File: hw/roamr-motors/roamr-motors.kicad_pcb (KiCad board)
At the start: 2 copper layers, 115 x 55 mm, 82 parts, among them J1 USB_C_Receptacle_USB2.0_14P, J10 JST_XH_S2B-XH-A-1, J2 USB_C_Receptacle_USB2.0_14P, J3 JST_XH_S2B-XH-A-1, J4 JST_XH_S2B-XH-A-1, J5 JST_PH_B3B-PH-SM4-TB, J6 JST_PH_B3B-PH-SM4-TB, J7 JST_SH_BM06B-SRSS-TB, J8 JST_SH_BM06B-SRSS-TB, J9 JST_XH_S2B-XH-A-1, U1 DRV8316CRRGFR, U2 DRV8316CRRGFR, U3 ESP32-S3-WROOM-1, U4 CP2102N-A02-GQFN28, U5 SGM2212-3.3XKC3G_TR

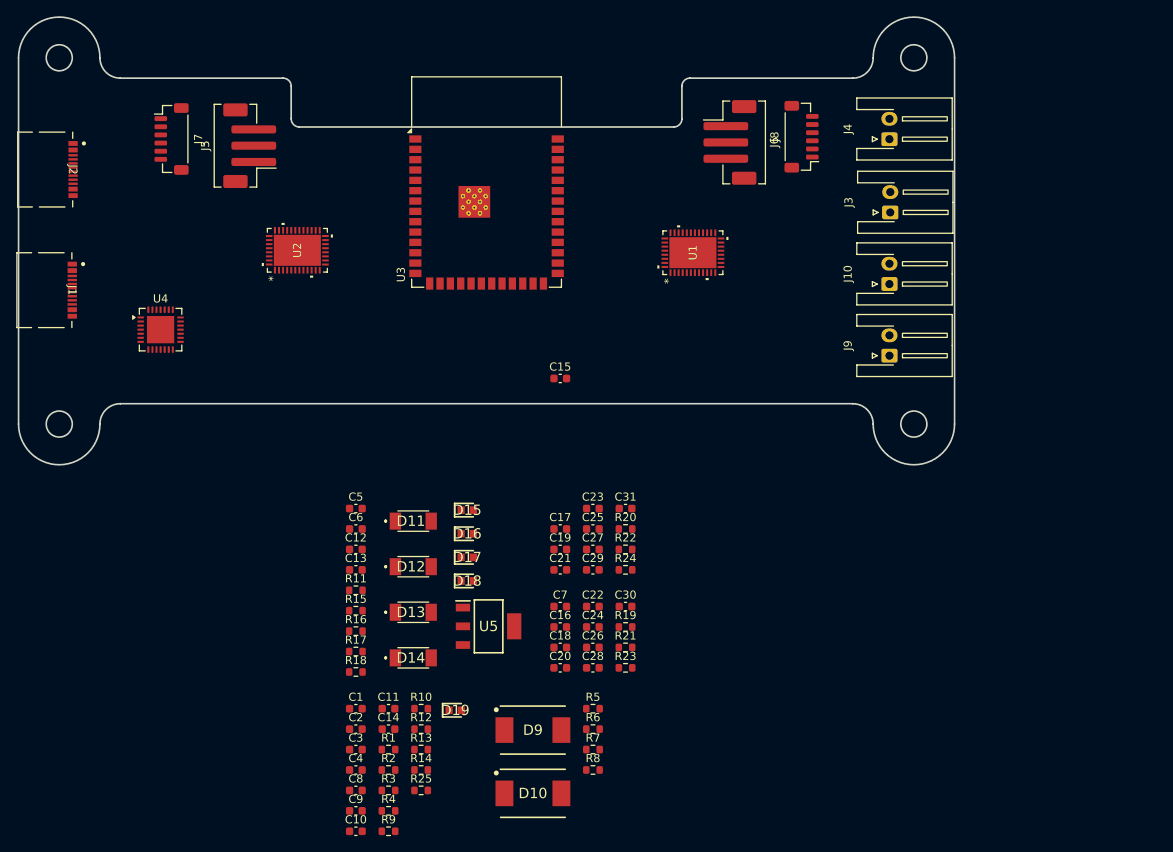
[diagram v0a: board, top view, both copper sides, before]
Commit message: added all footprints, starting layout properly
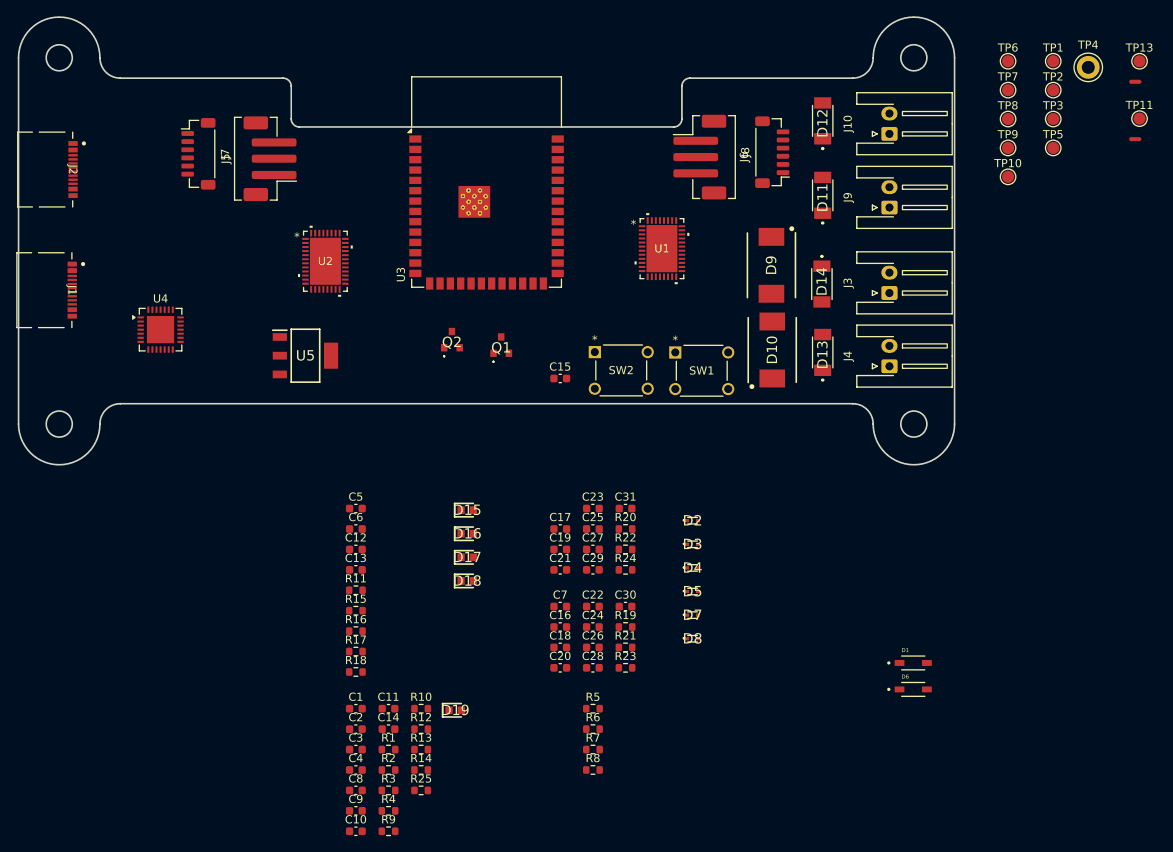
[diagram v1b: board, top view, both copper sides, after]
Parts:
- added D1: 1N5819HW-7-F, 1N5819HW_7_F:SOD3715X145N, F.Cu at (199.4, 146.7)
- added D2: LESD5D5.0CT1G, LESD5D5.0CT1G:LESD5D50CT1G, F.Cu at (172.3, 129.2)
- added D3: LESD5D5.0CT1G, LESD5D5.0CT1G:LESD5D50CT1G, F.Cu at (172.3, 132.1)
- added D4: LESD5D5.0CT1G, LESD5D5.0CT1G:LESD5D50CT1G, F.Cu at (172.3, 135.0)
- added D5: LESD5D5.0CT1G, LESD5D5.0CT1G:LESD5D50CT1G, F.Cu at (172.3, 137.9)
- added D6: 1N5819HW-7-F, 1N5819HW_7_F:SOD3715X145N, F.Cu at (199.4, 149.9)
- added D7: LESD5D5.0CT1G, LESD5D5.0CT1G:LESD5D50CT1G, F.Cu at (172.3, 140.8)
- added D8: LESD5D5.0CT1G, LESD5D5.0CT1G:LESD5D50CT1G, F.Cu at (172.3, 143.7)
- added NT1: NetTie_2, NetTie:NetTie-2_SMD_Pad0.5mm, F.Cu at (226.7, 82.3)
- added NT2: NetTie_2, NetTie:NetTie-2_SMD_Pad0.5mm, F.Cu at (226.7, 75.2)
- added Q1: L8050QLT1G, L8050QLT1G:L8050QLT1G, F.Cu at (148.8, 107.6)
- added Q2: L8050QLT1G, L8050QLT1G:L8050QLT1G, F.Cu at (142.8, 106.9)
- added SW1: 1825910-6, 1825910_6:SW4_1825910-B_TEC, F.Cu at (176.7, 113.0)
- added SW2: 1825910-6, 1825910_6:SW4_1825910-B_TEC, F.Cu at (166.8, 113.0)
- added TP1: TestPoint, TestPoint:TestPoint_Pad_D1.5mm, F.Cu at (216.6, 72.7)
- added TP10: TestPoint, TestPoint:TestPoint_Pad_D1.5mm, F.Cu at (211.1, 86.9)
- added TP11: TestPoint, TestPoint:TestPoint_Pad_D1.5mm, F.Cu at (227.2, 79.8)
- added TP13: TestPoint, TestPoint:TestPoint_Pad_D1.5mm, F.Cu at (227.2, 72.7)
- added TP2: TestPoint, TestPoint:TestPoint_Pad_D1.5mm, F.Cu at (216.6, 76.3)
- added TP3: TestPoint, TestPoint:TestPoint_Pad_D1.5mm, F.Cu at (216.6, 79.8)
- added TP4: TestPoint, TestPoint:TestPoint_Keystone_5005-5009_Compact, F.Cu at (220.9, 73.5)
- added TP5: TestPoint, TestPoint:TestPoint_Pad_D1.5mm, F.Cu at (216.6, 83.4)
- added TP6: TestPoint, TestPoint:TestPoint_Pad_D1.5mm, F.Cu at (211.1, 72.7)
- added TP7: TestPoint, TestPoint:TestPoint_Pad_D1.5mm, F.Cu at (211.1, 76.3)
- added TP8: TestPoint, TestPoint:TestPoint_Pad_D1.5mm, F.Cu at (211.1, 79.8)
- added TP9: TestPoint, TestPoint:TestPoint_Pad_D1.5mm, F.Cu at (211.1, 83.4)
- C8: value 1uF (10%) -> 1uF
- moved D12 74.4 mm to (188.3, 80.0), turned to 90 degrees
- moved D14 68.0 mm to (188.2, 100.1), turned to -90 degrees
- moved D11 64.3 mm to (188.3, 89.2), turned to 90 degrees
- moved D9 64.2 mm to (182.0, 97.8), turned to -90 degrees
- moved D10 61.9 mm to (182.1, 108.2), turned to 90 degrees
- moved D13 59.6 mm to (188.3, 108.5), turned to 90 degrees
- moved U5 40.1 mm to (124.8, 108.9)
- moved J4 27.9 mm to (196.5, 110.2)
- moved J10 18.4 mm to (196.5, 81.7)
- moved J9 18.2 mm to (196.5, 90.7)
- moved J3 9.90 mm to (196.5, 101.2)
- moved J6 4.11 mm to (173.2, 84.5)
- moved J8 4.07 mm to (182.1, 83.9)
- moved U1 3.83 mm to (168.5, 95.7), turned to 0 degrees
- moved J7 3.77 mm to (111.6, 84.1)
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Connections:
- C24 pad 1: /PWM1_M1 -> /ISENSE1_M1
- C26 pad 1: /PWM2_M1 -> /ISENSE2_M1
- C28 pad 1: /PWM3_M1 -> /ISENSE3_M1
- R12 pad 2: /Microcontroller/CHIP_PU -> /Microcontroller/MCU_EN
- R19 pad 2: /PWM1_M1 -> /ISENSE1_M1
- R21 pad 2: /PWM2_M1 -> /ISENSE2_M1
- R23 pad 2: /PWM3_M1 -> /ISENSE3_M1
- U1 pad 13: /CS_DR_M1 -> /MOUT1_M1
- U1 pad 14: /CS_DR_M1 -> /MOUT1_M1
- U1 pad 16: /SPI_MOSI -> /MOUT2_M1
- U1 pad 17: /SPI_MOSI -> /MOUT2_M1
- U1 pad 19: /SPI_MISO -> /MOUT3_M1
- U1 pad 20: /SPI_MISO -> /MOUT3_M1
- U1 pad 27: /ISENSE1_M1 -> /PWM1_M1
- U1 pad 29: /ISENSE2_M1 -> /PWM2_M1
- U1 pad 31: /ISENSE3_M1 -> /PWM3_M1
- U1 pad 33: /MOUT3_M1 -> /SPI_MISO
- U1 pad 34: /MOUT2_M1 -> /SPI_MOSI
- U1 pad 35: /BLDC Driver 1/SPI_CLK -> /SPI_CLK
- U1 pad 36: /MOUT1_M1 -> /CS_DR_M1
- U3 pad 26: /PWM3_M3 -> /PWM3_M1
- U3 pad 35: /PWM2_M2 -> /PWM2_M1

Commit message: some more layout
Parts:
- J1, J2: value USB_C_Receptacle_USB2.0_14P -> USB4215-03-A
- TP1, TP10, TP11, TP13, TP2, TP3, TP5, TP6, TP7, TP8, TP9: moved to B.Cu
- moved TP13 121.7 mm to (109.1, 101.8), turned to 180 degrees
- moved TP4 119.0 mm to (102.1, 79.1)
- moved D6 116.8 mm to (98.5, 91.1), turned to 90 degrees
- moved TP5 115.3 mm to (104.6, 110.5), turned to 90 degrees
- moved D1 112.8 mm to (98.5, 96.5), turned to -90 degrees
- moved TP3 112.7 mm to (108.2, 110.5), turned to 90 degrees
- moved TP2 110.4 mm to (111.7, 110.5), turned to 90 degrees
- moved TP1 108.2 mm to (115.2, 110.5), turned to 90 degrees
- moved NT1 96.6 mm to (142.7, 129.9)
- moved NT2 96.6 mm to (142.7, 122.9)
- moved TP7 96.1 mm to (119.8, 106.5), turned to 90 degrees
- moved TP10 94.4 mm to (119.7, 110.7), turned to 90 degrees
- moved TP6 94.0 mm to (123.3, 106.5), turned to 90 degrees
- moved D8 93.4 mm to (98.5, 86.5), turned to 90 degrees
- moved D5 92.4 mm to (98.2, 82.7), turned to -90 degrees
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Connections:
- D1 pad A: (no net) -> VBUS_5V_1
- D1 pad C: (no net) -> VSYS_5V
- D6 pad A: (no net) -> VBUS_5V_2
- D6 pad C: (no net) -> VSYS_5V
- J1 pad A1/B12: (no net) -> GND
- J1 pad A4/B9: (no net) -> VBUS_5V_1
- J1 pad A8: (no net) -> unconnected-(J1-SBU1-PadA8)
- J1 pad B1/A12: (no net) -> GND
- J1 pad B4/A9: (no net) -> VBUS_5V_1
- J1 pad B8: (no net) -> unconnected-(J1-SBU2-PadB8)
- J2 pad A1/B12: (no net) -> GND
- J2 pad A4/B9: (no net) -> VBUS_5V_2
- J2 pad A8: (no net) -> unconnected-(J2-SBU1-PadA8)
- J2 pad B1/A12: (no net) -> GND
- J2 pad B4/A9: (no net) -> VBUS_5V_2
- J2 pad B8: (no net) -> unconnected-(J2-SBU2-PadB8)
- Q1 pad 1: (no net) -> Net-(Q1-B)
- Q1 pad 2: (no net) -> /Microcontroller/RTS
- Q1 pad 3: (no net) -> Net-(Q1-C)
- Q2 pad 1: (no net) -> Net-(Q2-B)
- Q2 pad 2: (no net) -> /Microcontroller/DTR
- Q2 pad 3: (no net) -> Net-(Q2-C)
- R12 pad 1: Net-(Q1-PadC) -> Net-(Q1-C)
- R13 pad 1: Net-(Q2-PadC) -> Net-(Q2-C)
- R2 pad 2: Net-(Q1-PadB) -> Net-(Q1-B)
- R3 pad 2: Net-(Q2-PadB) -> Net-(Q2-B)
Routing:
- net /Microcontroller/MCU_EN: track 0.00 -> 54.7 mm, vias 0 -> 3
- net /USB_P: track 0.00 -> 50.6 mm, vias 0 -> 2
- net /USB_N: track 0.00 -> 50.0 mm, vias 0 -> 2
- net ESP_3V3: track 0.00 -> 38.9 mm, vias 0 -> 2
- net VSYS_3V3: track 0.00 -> 20.0 mm, vias 0 -> 15
- net GND: track 0.00 -> 17.2 mm, vias 0 -> 5
- net /PWM3_M2: track 0.00 -> 17.2 mm, vias 0 -> 2
- net /MOUT3_M1: track 0.00 -> 16.2 mm
- net /Microcontroller/GPIO0_BOOT: track 0.00 -> 15.6 mm
- net /PWM2_M2: track 0.00 -> 15.5 mm, vias 0 -> 2
- net /PWM1_M2: track 0.00 -> 14.0 mm, vias 0 -> 2
- net /MOUT2_M1: track 0.00 -> 13.9 mm
- net /USB_UART_P: track 0.00 -> 10.8 mm, vias 0 -> 2
- net VBUS_5V_1: track 0.00 -> 10.5 mm
- net /USB_UART_N: track 0.00 -> 9.91 mm, vias 0 -> 2
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- added copper zone on F.Cu, net GND
- added copper zone on In1.Cu, net GND
- added copper zone on In2.Cu, net GND
- added copper zone on F.Cu, net VOUT_12V
- added copper zone on F.Cu, net VOUT_5V
- added copper zone on B.Cu, net VSYS_12V
- added copper zone on F.Cu, net VSYS_12V
- added copper zone on F.Cu, net VSYS_3V3
- added copper zone on In2.Cu, net VSYS_3V3
- added copper zone on F.Cu, net VSYS_5V
- added copper zone on In2.Cu, net VSYS_5V
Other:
- copper layers 2 -> 4

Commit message: more layout, i think i get do it on one side
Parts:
- removed the C9 at (130.9, 164.8)
- C15: renamed from C16; value 47uH -> 47uF
- C19: renamed from C22; footprint Capacitor_SMD:C_0603_1608Metric -> RVT1E100M0405:RVT1E100M0405
- C24: renamed from C17; value 47uH -> 47uF
- C28: renamed from C23; footprint Capacitor_SMD:C_0603_1608Metric -> RVT1E100M0405:RVT1E100M0405
- C5: renamed from C2; value 10uF -> 4.7uF
- D1: renamed from D9; value D_TVS -> SMLJ12A-R
- D4: renamed from D10; value D_TVS -> SMLJ12A-R
- moved R3 96.5 mm to (100.4, 81.5), turned to 90 degrees
- moved R4 92.7 mm to (100.5, 88.8), turned to -90 degrees
- moved R1 80.2 mm to (100.4, 98.7), turned to 90 degrees
- moved R2 78.2 mm to (98.1, 107.1), turned to -90 degrees
- moved R14 70.6 mm to (101.8, 105.0), turned to 180 degrees
- moved R10 63.6 mm to (106.6, 105.0), turned to 180 degrees
- moved R11 60.0 mm to (104.2, 105.8), turned to -90 degrees
- moved C19 59.1 mm to (124.0, 92.9), turned to 90 degrees
- moved R15 58.9 mm to (101.8, 106.6)
- moved C17 58.0 mm to (123.0, 97.1)
- moved C15 54.3 mm to (122.3, 99.7), turned to 90 degrees
- moved C16 51.6 mm to (124.7, 98.8)
- moved NT2 40.3 mm to (176.5, 100.9)
- moved C26 40.1 mm to (174.7, 97.2)
- moved C28 37.6 mm to (176.6, 93.9)
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- renumbered C5 to C1, C8 to C10, C10 to C11, C11 to C12, C20 to C13, C30 to C14, C7 to C16, C18 to C17, C24 to C18, C6 to C2, C26 to C20, C28 to C21, C21 to C22, C31 to C23, C15 to C25, C19 to C26, C25 to C27, C27 to C29, C12 to C3, C29 to C30, C13 to C4, C14 to C6, C4 to C7, C3 to C8, C1 to C9, D6 to D10, D13 to D11, D14 to D12, D15 to D13, D16 to D14, D17 to D15, D18 to D16, D11 to D17, D12 to D18, D4 to D2, D5 to D3, D3 to D5, D7 to D6, D2 to D7, D1 to D9, J3 to J1, J8 to J10, J1 to J2, J2 to J3, J10 to J5, J5 to J6, J9 to J8, J6 to J9, R5 to R1, R14 to R10, R1 to R11, R2 to R12, R3 to R13, R9 to R14, R10 to R15, R12 to R16, R13 to R17, R25 to R18, R4 to R19, R6 to R2, R19 to R20, R23 to R22, R20 to R23, R22 to R24, R24 to R25, R7 to R3, R8 to R4, R15 to R5, R16 to R6, R11 to R7, R17 to R8, R18 to R9, TP13 to TP12, TP5 to TP3, TP3 to TP4, TP4 to TP5, U5 to U1, U4 to U2, U1 to U4, U2 to U5
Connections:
- C18 pad 2: GND -> AGND
- C20 pad 2: GND -> AGND
- C21 pad 2: GND -> AGND
- C27 pad 2: GND -> AGND
- C29 pad 2: GND -> AGND
- C30 pad 2: GND -> AGND
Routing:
- net VOUT_5V: track 0.00 -> 92.8 mm, vias 0 -> 3
- net /Microcontroller/UART0_RXD: track 0.00 -> 68.9 mm, vias 0 -> 2
- net /Microcontroller/UART0_TXD: track 0.00 -> 67.3 mm, vias 0 -> 2
- net VSYS_3V3: track 20.0 -> 39.4 mm, vias 15 -> 17
- net /MOUT1_M2: track 0.00 -> 17.8 mm, vias 0 -> 2
- net GND: track 17.2 -> 34.8 mm, vias 5 -> 8
- net /MOUT2_M2: track 0.00 -> 12.9 mm, vias 0 -> 2
- net /MOUT3_M2: track 0.00 -> 10.8 mm
- net AGND: track 0.00 -> 6.97 mm, vias 0 -> 4
- net Net-(J2-CC2): track 0.00 -> 6.01 mm, vias 0 -> 2
- net Net-(J3-CC1): track 0.00 -> 5.63 mm
- net VBUS_5V_1: track 10.5 -> 16.0 mm
- net Net-(U5A-SOC): track 0.00 -> 5.35 mm
- net Net-(J2-CC1): track 0.00 -> 4.92 mm, vias 0 -> 2
- net Net-(J3-CC2): track 0.00 -> 4.49 mm
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- added copper zone on F.Cu, net AGND

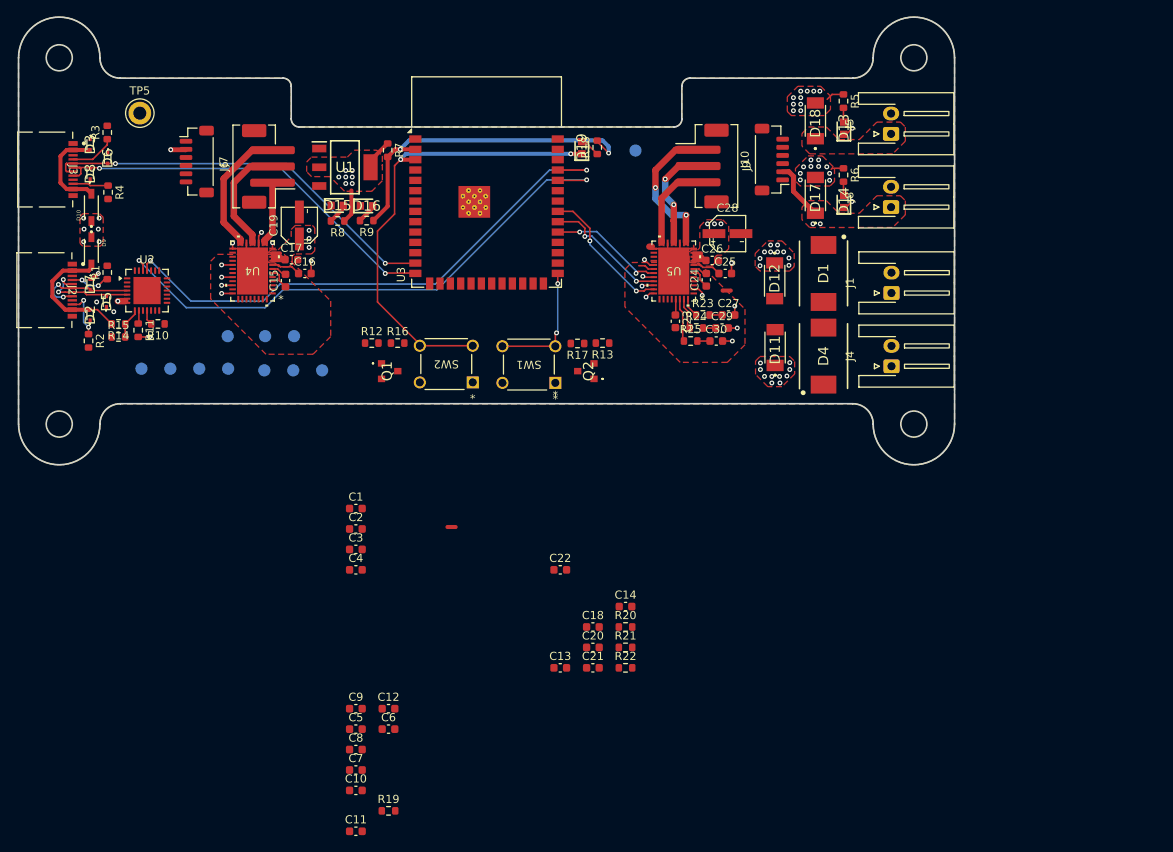
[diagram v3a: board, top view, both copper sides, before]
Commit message: layout done except i need to add two fuses
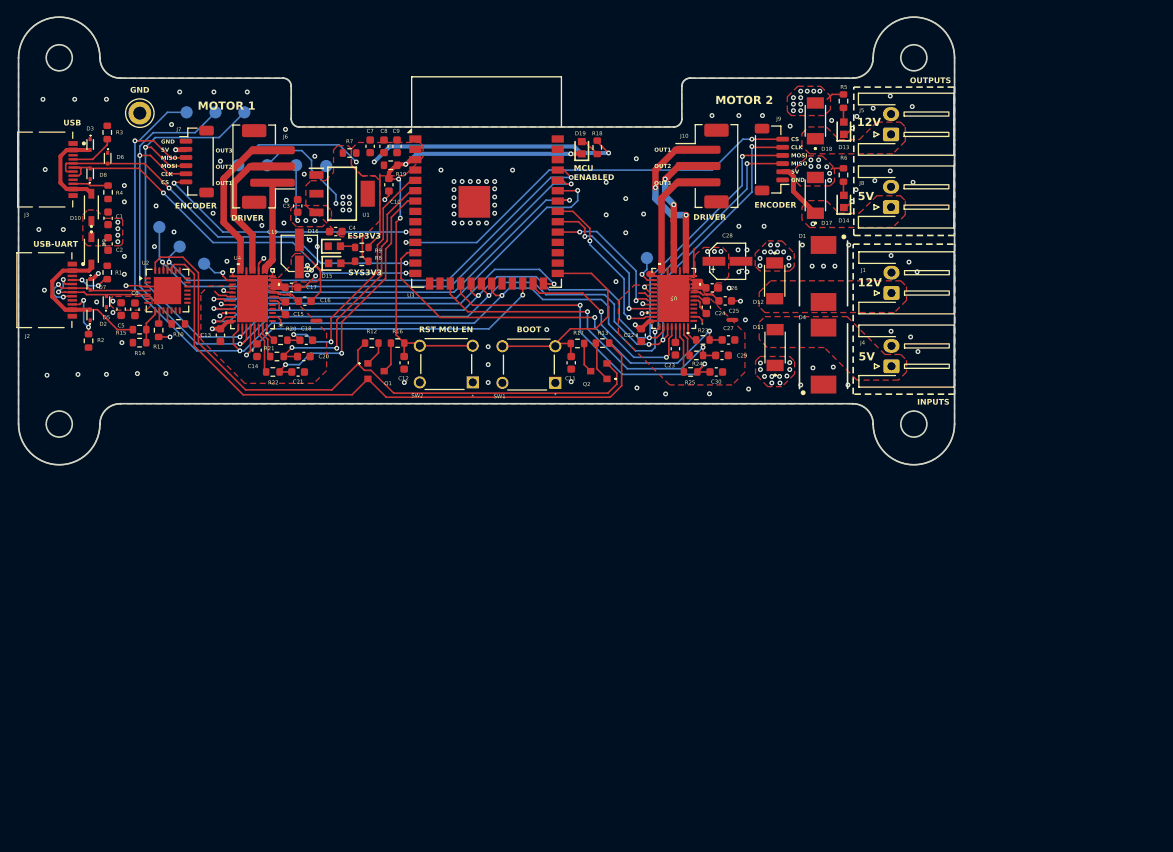
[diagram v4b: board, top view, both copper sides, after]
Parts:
- moved R19 79.3 mm to (135.2, 85.5)
- moved C7 76.6 mm to (132.7, 83.2), turned to 90 degrees
- moved C10 74.5 mm to (135.0, 87.9), turned to -90 degrees
- moved C8 74.2 mm to (134.4, 83.2), turned to 90 degrees
- moved C9 69.3 mm to (136.0, 83.2), turned to 90 degrees
- moved C11 63.3 mm to (157.4, 109.8), turned to -90 degrees
- moved C6 60.3 mm to (103.8, 103.2), turned to -90 degrees
- moved C5 59.1 mm to (102.1, 103.2), turned to -90 degrees
- moved C13 58.4 mm to (114.3, 106.4), turned to -90 degrees
- moved R22 56.6 mm to (120.8, 110.9)
- moved R21 55.8 mm to (121.2, 109.0)
- moved C14 55.2 mm to (118.8, 108.2), turned to -90 degrees
- moved R20 55.1 mm to (121.7, 107.0)
- moved TP11 54.8 mm to (112.3, 97.6)
- moved TP12 52.4 mm to (166.7, 96.9)
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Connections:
- C13 pad 2: AGND -> /BLDC Driver 1/AGND
- C14 pad 2: AGND -> /BLDC Driver 1/AGND
- C18 pad 2: AGND -> /BLDC Driver 1/AGND
- C20 pad 2: AGND -> /BLDC Driver 1/AGND
- C21 pad 2: AGND -> /BLDC Driver 1/AGND
- C22 pad 2: AGND -> /BLDC Driver 2/AGND
- C23 pad 2: AGND -> /BLDC Driver 2/AGND
- C27 pad 2: AGND -> /BLDC Driver 2/AGND
- C29 pad 2: AGND -> /BLDC Driver 2/AGND
- C30 pad 2: AGND -> /BLDC Driver 2/AGND
- NT1 pad 1: AGND -> /BLDC Driver 1/AGND
- NT2 pad 1: AGND -> /BLDC Driver 2/AGND
- U4 pad 2: AGND -> /BLDC Driver 1/AGND
- U4 pad 26: AGND -> /BLDC Driver 1/AGND
- U5 pad 2: AGND -> /BLDC Driver 2/AGND
- U5 pad 26: AGND -> /BLDC Driver 2/AGND
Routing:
- net /SPI_CLK: track 0.00 -> 148.2 mm, vias 0 -> 6
- net /SPI_MOSI: track 0.00 -> 146.8 mm, vias 0 -> 5
- net /SPI_MISO: track 0.00 -> 146.5 mm, vias 0 -> 5
- net /Microcontroller/DTR: track 0.00 -> 79.0 mm
- net /Microcontroller/RTS: track 0.00 -> 75.8 mm
- net /PWM2_M1: track 0.00 -> 56.3 mm, vias 0 -> 2
- net /CS_ENC_M2: track 0.00 -> 52.7 mm, vias 0 -> 2
- net /PWM1_M1: track 0.00 -> 52.6 mm, vias 0 -> 2
- net /ISENSE1_M2: track 1.55 -> 51.7 mm, vias 0 -> 2
- net /PWM3_M1: track 0.00 -> 49.1 mm, vias 0 -> 2
- net /CS_DR_M1: track 0.00 -> 42.1 mm, vias 0 -> 2
- net /ISENSE2_M2: track 1.55 -> 41.0 mm, vias 0 -> 2
- net /ISENSE3_M2: track 1.55 -> 40.7 mm, vias 0 -> 2
- net /CS_ENC_M1: track 0.00 -> 33.7 mm, vias 0 -> 2
- net /ISENSE3_M1: track 0.00 -> 33.2 mm, vias 0 -> 2
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- added copper zone on F.Cu, net /BLDC Driver 1/AGND
- added copper zone on F.Cu, net /BLDC Driver 2/AGND
- added copper zone on F.Cu, net ESP_3V3
- added copper zone on F.Cu, net VIN_12V
- added copper zone on F.Cu, net VIN_5V
- removed copper zone on F.Cu, net AGND
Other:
- board text added: "12V"
- board text added: "5V"
- board text added: "BOOT"
- board text added: "CLK"
- board text added: "CS"
- board text added: "DRIVER"
- board text added: "ENCODER"
- board text added: "ESP3V3"
- board text added: "ESP_3V3"
- board text added: "GND"
- board text added: "INPUTS"
- board text added: "M1 FAULT"
- board text added: "M2 FAULT"
- board text added: "MCU ENABLED"
- board text added: "MISO"
- board text added: "MOSI"
- board text added: "MOTOR 1"
- board text added: "MOTOR 2"
- board text added: "OUT1"
- board text added: "OUT2"
- board text added: "OUT3"
- board text added: "OUTPUTS"
- board text added: "RST MCU EN"
- board text added: "SYS3V3"
- board text added: "UART RX"
- board text added: "UART TX"
- board text added: "USB"
- board text added: "USB-UART"
- board text added: "VSYS_12V"
- board text added: "VSYS_3V3"
- board text added: "VSYS_5V"
